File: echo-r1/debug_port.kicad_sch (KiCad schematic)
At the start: 4 parts, among them J7 PM254-1-06-W-8.5

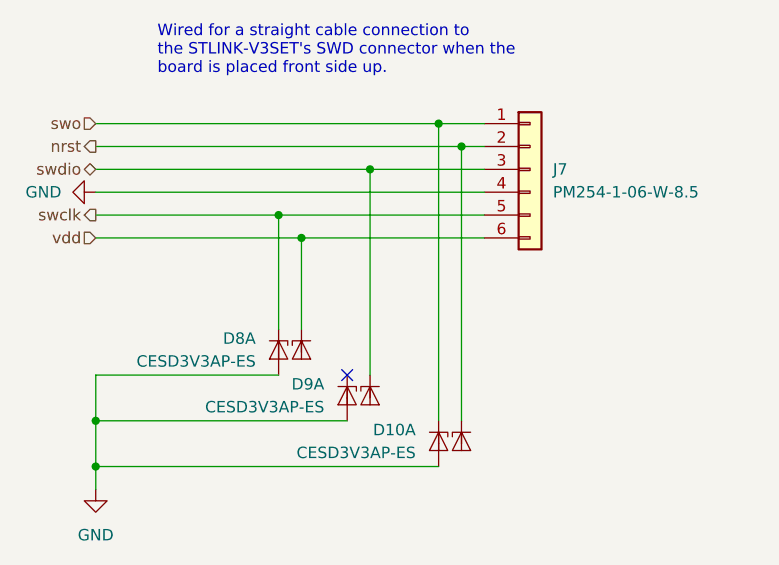
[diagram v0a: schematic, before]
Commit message: WIP redesign with STM32H7R3Z8J6
The H7R3 has a bunch of features that greatly simplify the design:
support for HyperRAM, which requires far fewer pins than SDRAM and
is more power efficient; this frees up the FMC to interface with the
display in 8-bit 8080 MCU mode; and there is a built-in USB HS PHY,
removing the need for an external PHY.

The huge reduction in signal count allows for a smaller pin count
package -- only 144 pins. HyperRAM only comes in BGA packages so it
makes sense to also use the UFBGA-144 package for the CPU, which
takes up less than 1/4 of the board area of an LQFP-176 package.
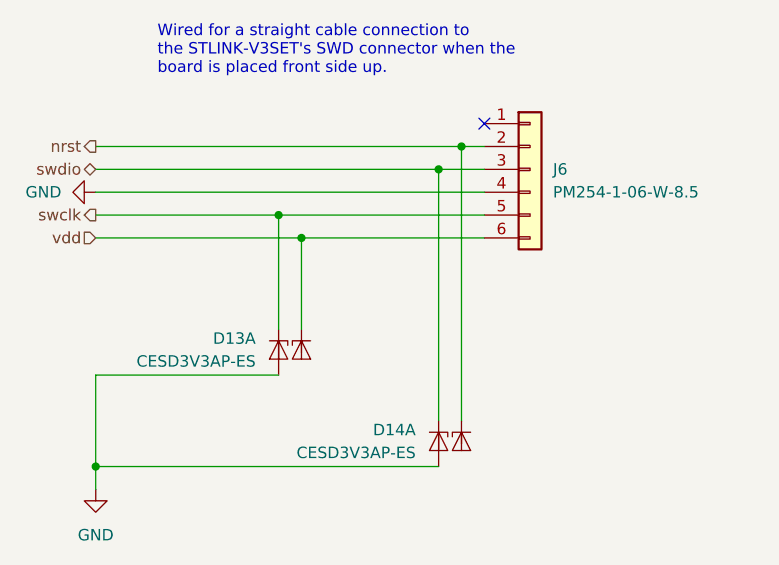
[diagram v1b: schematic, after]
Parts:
- removed D9: CESD3V3AP-ES, Package_TO_SOT_SMD:SOT-23, symbol echoplayer:CESD3V3AP-ES
- renumbered D8 to D13, D10 to D14, J7 to J6
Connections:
- net swdio: now also D14.1 (K1)
- net swo: no longer names the net of J6.1 (Pin_1)
- net swo: no longer D14.1 (K1)
